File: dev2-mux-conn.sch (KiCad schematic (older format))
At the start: 9 parts, among them J26 Device 2, U16 TS12A44514, U17 TS12A44514, U20 MAX4533, U50 74LS32, U54 LTC1391, U55 LTC1391, U56 LTC1391

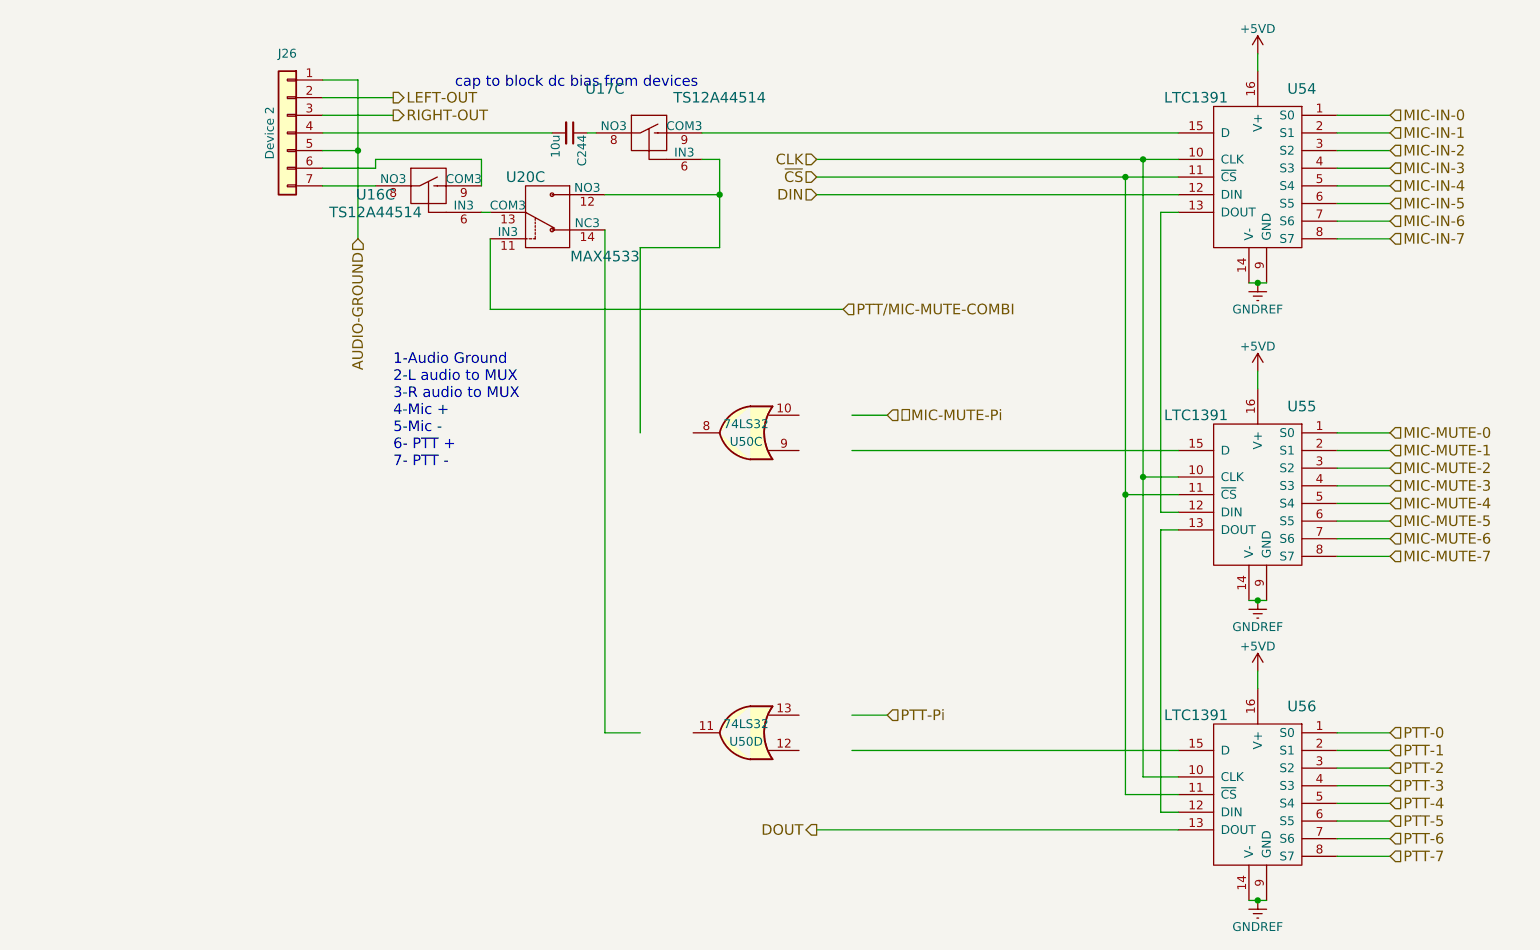
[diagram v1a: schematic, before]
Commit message: Updating power + libraries
- Reannotated all parts
- Migrated to new OR gate library
- Reorganized power sheet
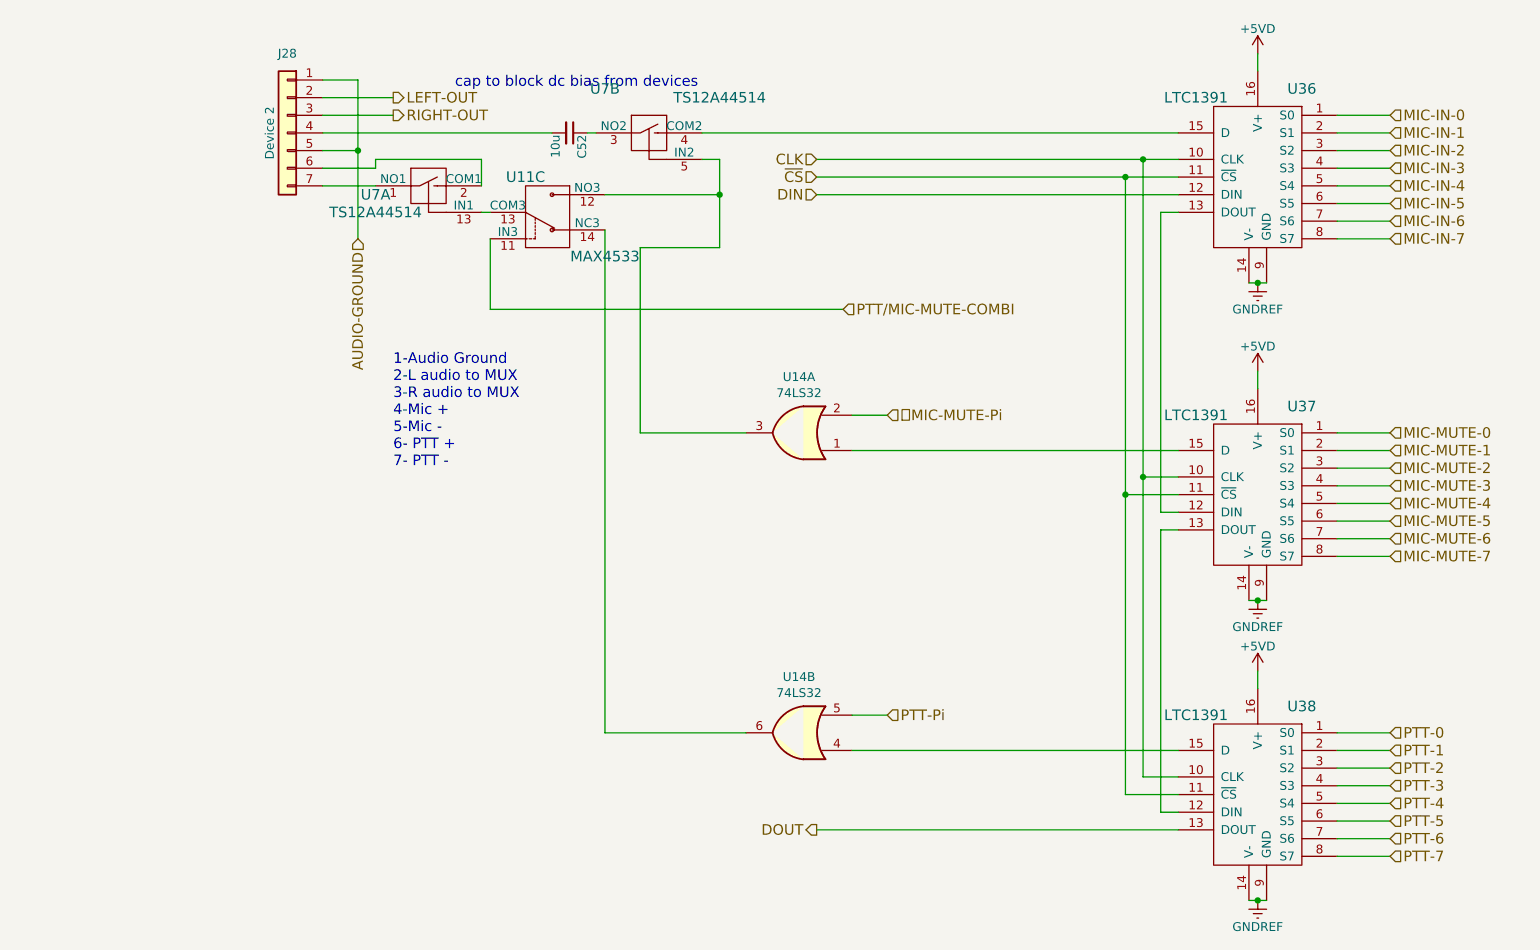
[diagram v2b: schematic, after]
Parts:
- removed U50: 74LS32, SMD_Packages:SSOP-14, symbol 74LS32
- added U14: 74LS32, symbol 74LS32
- renumbered C244 to C52, J26 to J28, U20 to U11, U54 to U36, U55 to U37, U56 to U38, U17 to U7, U16 to U7
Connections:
- wire segments 76 -> 77
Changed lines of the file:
@@
-EESchema Schematic File Version 2
+EESchema Schematic File Version 3
 LIBS:SW-Texas
 LIBS:power
@@
 $Descr USLetter 11000 8500
 encoding utf-8
-Sheet 16 15
+Sheet 7 15
 Title ""
 Date ""
@@
 $EndDescr
 $Comp
-L Conn_01x07 J26
+L Conn_01x07 J28
 U 1 1 58EAA0D9
 P 900 1150
-F 0 "J26" H 900 1600 50  0000 C CNN
+F 0 "J28" H 900 1600 50  0000 C CNN
 F 1 "Device 2" V 1000 1150 50  0000 C CNN
 F 2 "Pin_Headers:Pin_Header_Straight_1x07_Pitch2.54mm" H 900 1150 50  0001 C CNN
@@
 $Comp
 L TS12A44514 U?
-U 3 1 58EAA0E5
+U 2 1 58EAA0E5
 P 2950 1150
 AR Path="/58DEDA38/58EAA0E5" Ref="U?"  Part="1"
 AR Path="/58DEDA38/58E9E25B/58EAA0E5" Ref="U?"  Part="1"
-AR Path="/58DEDA38/58E9E991/58EAA0E5" Ref="U17"  Part="3"
-F 0 "U17" H 2700 1400 60  0000 C CNN
+AR Path="/58DEDA38/58E9E991/58EAA0E5" Ref="U7"  Part="2"
+F 0 "U7" H 2700 1400 60  0000 C CNN
 F 1 "TS12A44514" H 3350 1350 60  0000 C CNN
 F 2 "Housings_SSOP:TSSOP-14_4.4x5mm_Pitch0.65mm" H 3450 2450 60  0001 C CNN
@@
 F 7 "TSSOP14" H 3250 2350 60  0001 C CNN "Package ID"
 F 8 "0.00@0" H 3000 2150 60  0001 C CNN "Pricing"
-	3    2950 1150
+	2    2950 1150
 	1    0    0    -1
 $EndComp
 $Comp
 L TS12A44514 U?
-U 3 1 58EAA0F1
+U 1 1 58EAA0F1
 P 1700 1450
 AR Path="/58DEDA38/58EAA0F1" Ref="U?"  Part="1"
 AR Path="/58DEDA38/58E9E25B/58EAA0F1" Ref="U?"  Part="1"
-AR Path="/58DEDA38/58E9E991/58EAA0F1" Ref="U16"  Part="3"
-F 0 "U16" H 1400 1400 60  0000 C CNN
+AR Path="/58DEDA38/58E9E991/58EAA0F1" Ref="U7"  Part="1"
+F 0 "U7" H 1400 1400 60  0000 C CNN
 F 1 "TS12A44514" H 1400 1300 60  0000 C CNN
 F 2 "Housings_SSOP:TSSOP-14_4.4x5mm_Pitch0.65mm" H 2200 2750 60  0001 C CNN
@@
 F 7 "TSSOP14" H 2000 2650 60  0001 C CNN "Package ID"
 F 8 "0.00@0" H 1750 2450 60  0001 C CNN "Pricing"
-	3    1700 1450
-	1    0    0    -1
-$EndComp
-$Comp
-L C_Small C244
+	1    1700 1450
+	1    0    0    -1
+$EndComp
+$Comp
+L C_Small C52
 U 1 1 58EAA0F8
 P 2500 1150
-F 0 "C244" H 2510 1220 50  0000 L CNN
+F 0 "C52" H 2510 1220 50  0000 L CNN
 F 1 "10u" H 2510 1070 50  0000 L CNN
 F 2 "Capacitors_SMD:C_0603" H 2500 1150 50  0001 C CNN
@@
 AUDIO-GROUND
 $Comp
-L LTC1391 U54
+L LTC1391 U36
 U 1 1 58EAA108
 P 6400 1400
-F 0 "U54" H 6150 1900 60  0000 C CNN
+F 0 "U36" H 6150 1900 60  0000 C CNN
 F 1 "LTC1391" H 6750 1850 60  0000 C CNN
 F 2 "Housings_SSOP:SSOP-16_3.9x4.9mm_Pitch0.635mm" H 6500 2650 60  0001 C CNN
@@
 DOUT
 $Comp
-L +5VD #PWR0205
+L +5VD #PWR072
 U 1 1 58EAA113
 P 6400 700
-F 0 "#PWR0205" H 6400 550 50  0001 C CNN
+F 0 "#PWR072" H 6400 550 50  0001 C CNN
 F 1 "+5VD" H 6400 840 50  0000 C CNN
 F 2 "" H 6400 700 50  0001 C CNN
@@
 $EndComp
 $Comp
-L GNDREF #PWR0206
+L GNDREF #PWR073
 U 1 1 58EAA119
 P 6400 2000
-F 0 "#PWR0206" H 6400 1750 50  0001 C CNN
+F 0 "#PWR073" H 6400 1750 50  0001 C CNN
 F 1 "GNDREF" H 6400 1850 50  0000 C CNN
 F 2 "" H 6400 2000 50  0001 C CNN
@@
 Text HLabel 7150 1750 2    60   Input ~ 0
 MIC-IN-7
-$Comp
-L 74LS32 U50
-U 3 1 58EAA127
-P 3500 2850
-F 0 "U50" H 3500 2900 50  0000 C CNN
-F 1 "74LS32" H 3500 2800 50  0000 C CNN
-F 2 "SMD_Packages:SSOP-14" H 3500 2850 50  0001 C CNN
-F 3 "" H 3500 2850 50  0001 C CNN
-	3    3500 2850
-	-1   0    0    1
-$EndComp
-$Comp
-L 74LS32 U50
-U 4 1 58EAA12E
-P 3500 4550
-F 0 "U50" H 3500 4600 50  0000 C CNN
-F 1 "74LS32" H 3500 4500 50  0000 C CNN
-F 2 "SMD_Packages:SSOP-14" H 3500 4550 50  0001 C CNN
-F 3 "" H 3500 4550 50  0001 C CNN
-F 4 "0.00@0" H 3500 4550 60  0001 C CNN "Pricing"
-	4    3500 4550
-	-1   0    0    1
-$EndComp
 Text HLabel 4300 2750 2    60   Input ~ 0
 MIC-MUTE-Pi
@@
 P 2350 1600
 AR Path="/58DEDA38/58E9E25B/58EAA13B" Ref="U?"  Part="1"
-AR Path="/58DEDA38/58E9E991/58EAA13B" Ref="U20"  Part="3"
-F 0 "U20" H 2450 1800 60  0000 C CNN
+AR Path="/58DEDA38/58E9E991/58EAA13B" Ref="U11"  Part="3"
+F 0 "U11" H 2450 1800 60  0000 C CNN
 F 1 "MAX4533" H 2000 1350 60  0000 C CNN
 F 2 "Housings_SSOP:SSOP-20_4.4x6.5mm_Pitch0.65mm" H 2450 2550 60  0001 C CNN
@@
 PTT-7
 $Comp
-L LTC1391 U55
+L LTC1391 U37
 U 1 1 58EAA156
 P 6400 3200
-F 0 "U55" H 6150 3700 60  0000 C CNN
+F 0 "U37" H 6150 3700 60  0000 C CNN
 F 1 "LTC1391" H 6750 3650 60  0000 C CNN
 F 2 "Housings_SSOP:SSOP-16_3.9x4.9mm_Pitch0.635mm" H 6500 4450 60  0001 C CNN
@@
 $EndComp
 $Comp
-L +5VD #PWR0207
+L +5VD #PWR074
 U 1 1 58EAA15D
 P 6400 2500
-F 0 "#PWR0207" H 6400 2350 50  0001 C CNN
+F 0 "#PWR074" H 6400 2350 50  0001 C CNN
 F 1 "+5VD" H 6400 2640 50  0000 C CNN
 F 2 "" H 6400 2500 50  0001 C CNN
@@
 $EndComp
 $Comp
-L GNDREF #PWR0208
+L GNDREF #PWR075
 U 1 1 58EAA163
 P 6400 3800
-F 0 "#PWR0208" H 6400 3550 50  0001 C CNN
+F 0 "#PWR075" H 6400 3550 50  0001 C CNN
 F 1 "GNDREF" H 6400 3650 50  0000 C CNN
 F 2 "" H 6400 3800 50  0001 C CNN
@@
 $EndComp
 $Comp
-L LTC1391 U56
+L LTC1391 U38
 U 1 1 58EAA16D
 P 6400 4900
-F 0 "U56" H 6150 5400 60  0000 C CNN
+F 0 "U38" H 6150 5400 60  0000 C CNN
 F 1 "LTC1391" H 6750 5350 60  0000 C CNN
 F 2 "Housings_SSOP:SSOP-16_3.9x4.9mm_Pitch0.635mm" H 6500 6150 60  0001 C CNN
@@
 $EndComp
 $Comp
-L +5VD #PWR0209
+L +5VD #PWR076
 U 1 1 58EAA174
 P 6400 4200
-F 0 "#PWR0209" H 6400 4050 50  0001 C CNN
+F 0 "#PWR076" H 6400 4050 50  0001 C CNN
 F 1 "+5VD" H 6400 4340 50  0000 C CNN
 F 2 "" H 6400 4200 50  0001 C CNN
@@
 $EndComp
 $Comp
-L GNDREF #PWR0210
+L GNDREF #PWR077
 U 1 1 58EAA17A
 P 6400 5500
-F 0 "#PWR0210" H 6400 5250 50  0001 C CNN
+F 0 "#PWR077" H 6400 5250 50  0001 C CNN
 F 1 "GNDREF" H 6400 5350 50  0000 C CNN
 F 2 "" H 6400 5500 50  0001 C CNN
@@
 	2900 1800 2900 2850
 Wire Wire Line
-	4100 2750 4300 2750
-Wire Wire Line
 	4100 4450 4300 4450
 Wire Wire Line
 	2700 1500 3350 1500
 Connection ~ 3350 1500
-Wire Wire Line
-	2900 4550 2700 4550
 Wire Wire Line
 	2700 4550 2700 1700
@@
 Text Notes 1500 3050 0    60   ~ 0
 1-Audio Ground\n2-L audio to MUX\n3-R audio to MUX\n4-Mic +\n5-Mic -\n6- PTT +\n7- PTT -
+Wire Wire Line
+	2700 4550 3500 4550
+$Comp
+L 74LS32 U?
+U 1 1 59D24FEE
+P 3800 2850
+AR Path="/58DEDA38/58E9E2BE/59D24FEE" Ref="U?"  Part="1"
+AR Path="/58DEDA38/58E9E991/59D24FEE" Ref="U14"  Part="1"
+F 0 "U14" H 3800 2533 50  0000 C CNN
+F 1 "74LS32" H 3800 2624 50  0000 C CNN
+F 2 "" H 3800 2850 50  0001 C CNN
+F 3 "" H 3800 2850 50  0001 C CNN
+	1    3800 2850
+	-1   0    0    1
+$EndComp
+Wire Wire Line
+	2900 2850 3500 2850
+$Comp
+L 74LS32 U?
+U 2 1 59D24FF6
+P 3800 4550
+AR Path="/58DEDA38/58E9E2BE/59D24FF6" Ref="U?"  Part="2"
+AR Path="/58DEDA38/58E9E9F4/59D24FF6" Ref="U?"  Part="2"
+AR Path="/58DEDA38/58E9E991/59D24FF6" Ref="U14"  Part="2"
+F 0 "U14" H 3800 4233 50  0000 C CNN
+F 1 "74LS32" H 3800 4324 50  0000 C CNN
+F 2 "" H 3800 4550 50  0001 C CNN
+F 3 "" H 3800 4550 50  0001 C CNN
+	2    3800 4550
+	-1   0    0    1
+$EndComp
+Wire Wire Line
+	4300 2750 4100 2750
 $EndSCHEMATC

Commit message: Updates during pcb layout
Added more net labels
moved switches and OR gates to +5V instead of +5VD
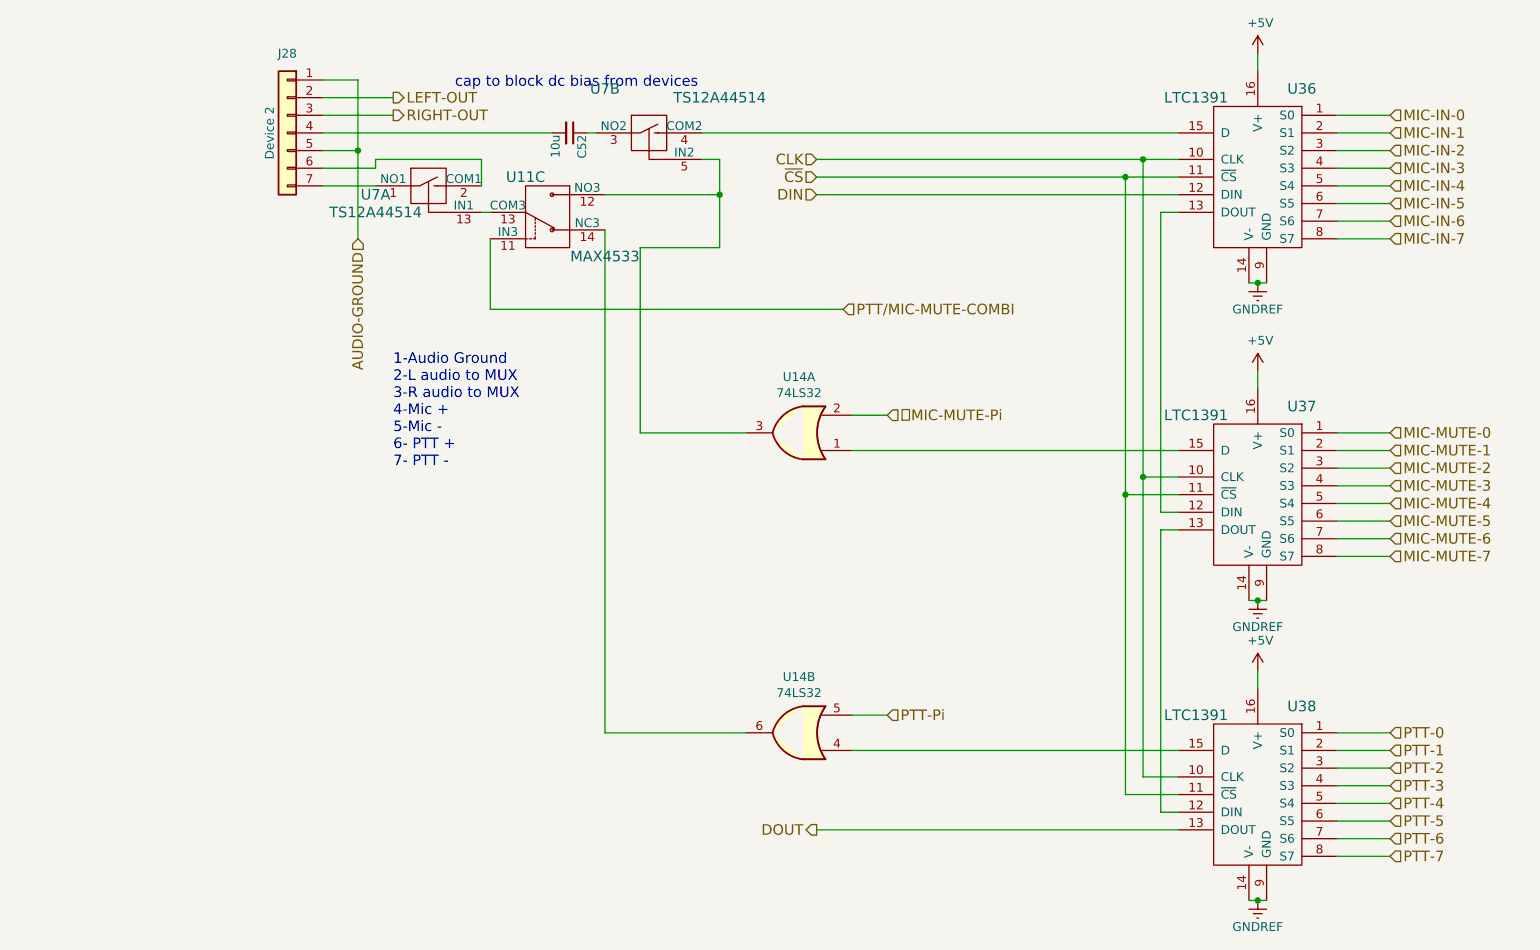
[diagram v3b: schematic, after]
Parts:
- J28: footprint Pin_Headers:Pin_Header_Straight_1x07_Pitch2.54mm -> SW-TEConn:3-794681-8
- U14: footprint (none) -> Housings_SSOP:SSOP-14_5.3x6.2mm_Pitch0.65mm
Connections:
- net +5VD renamed +5V
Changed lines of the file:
@@
 LIBS:SW-Diodes-Inc
 LIBS:interface
+LIBS:SW-gElectroMech
 LIBS:edc-mux-board-cache
 EELAYER 26 0
@@
 F 0 "J28" H 900 1600 50  0000 C CNN
 F 1 "Device 2" V 1000 1150 50  0000 C CNN
-F 2 "Pin_Headers:Pin_Header_Straight_1x07_Pitch2.54mm" H 900 1150 50  0001 C CNN
+F 2 "SW-TEConn:3-794681-8" H 900 1150 50  0001 C CNN
 F 3 "" H 900 1150 50  0001 C CNN
 F 4 "0.00@0" H 900 1150 60  0001 C CNN "Pricing"
@@
 Text HLabel 3900 5100 0    60   Output ~ 0
 DOUT
-$Comp
-L +5VD #PWR072
-U 1 1 58EAA113
-P 6400 700
-F 0 "#PWR072" H 6400 550 50  0001 C CNN
-F 1 "+5VD" H 6400 840 50  0000 C CNN
-F 2 "" H 6400 700 50  0001 C CNN
-F 3 "" H 6400 700 50  0001 C CNN
-	1    6400 700
-	1    0    0    -1
-$EndComp
 $Comp
 L GNDREF #PWR073
@@
 $EndComp
 $Comp
-L +5VD #PWR074
-U 1 1 58EAA15D
-P 6400 2500
-F 0 "#PWR074" H 6400 2350 50  0001 C CNN
-F 1 "+5VD" H 6400 2640 50  0000 C CNN
-F 2 "" H 6400 2500 50  0001 C CNN
-F 3 "" H 6400 2500 50  0001 C CNN
-	1    6400 2500
-	1    0    0    -1
-$EndComp
-$Comp
 L GNDREF #PWR075
 U 1 1 58EAA163
@@
 $EndComp
 $Comp
-L +5VD #PWR076
-U 1 1 58EAA174
-P 6400 4200
-F 0 "#PWR076" H 6400 4050 50  0001 C CNN
-F 1 "+5VD" H 6400 4340 50  0000 C CNN
-F 2 "" H 6400 4200 50  0001 C CNN
-F 3 "" H 6400 4200 50  0001 C CNN
-	1    6400 4200
-	1    0    0    -1
-$EndComp
-$Comp
 L GNDREF #PWR077
 U 1 1 58EAA17A
@@
 $EndComp
 Wire Wire Line
-	1300 850  1300 1750
+	1300 850  1300 1250
+Wire Wire Line
+	1300 1250 1300 1750
 Wire Wire Line
 	1100 850  1300 850
@@
 	3900 1500 5950 1500
 Wire Wire Line
-	3900 1400 5950 1400
-Wire Wire Line
-	3900 1300 5950 1300
+	3900 1400 5650 1400
+Wire Wire Line
+	5650 1400 5950 1400
+Wire Wire Line
+	3900 1300 5750 1300
+Wire Wire Line
+	5750 1300 5950 1300
 Wire Wire Line
 	6400 700  6400 800
 Wire Wire Line
-	6350 2000 6450 2000
+	6350 2000 6400 2000
+Wire Wire Line
+	6400 2000 6450 2000
 Wire Wire Line
 	6400 2000 6400 2000
 Connection ~ 6400 2000
 Wire Wire Line
-	3350 1300 3350 1800
+	3350 1300 3350 1500
+Wire Wire Line
+	3350 1500 3350 1800
 Wire Wire Line
 	3350 1800 2900 1800
@@
 	6400 2500 6400 2600
 Wire Wire Line
-	6350 3800 6450 3800
+	6350 3800 6400 3800
+Wire Wire Line
+	6400 3800 6450 3800
 Wire Wire Line
 	6400 3800 6400 3800
@@
 	6400 4200 6400 4300
 Wire Wire Line
-	6350 5500 6450 5500
+	6350 5500 6400 5500
+Wire Wire Line
+	6400 5500 6450 5500
 Wire Wire Line
 	6400 5500 6400 5500
 Connection ~ 6400 5500
 Wire Wire Line
-	5750 1300 5750 4800
+	5750 1300 5750 3100
+Wire Wire Line
+	5750 3100 5750 4800
 Connection ~ 5750 3100
 Connection ~ 5750 1300
 Wire Wire Line
-	5650 1400 5650 4900
+	5650 1400 5650 3200
+Wire Wire Line
+	5650 3200 5650 4900
 Connection ~ 5650 3200
 Connection ~ 5650 1400
@@
 F 0 "U14" H 3800 2533 50  0000 C CNN
 F 1 "74LS32" H 3800 2624 50  0000 C CNN
-F 2 "" H 3800 2850 50  0001 C CNN
+F 2 "Housings_SSOP:SSOP-14_5.3x6.2mm_Pitch0.65mm" H 3800 2850 50  0001 C CNN
 F 3 "" H 3800 2850 50  0001 C CNN
 	1    3800 2850
@@
 F 0 "U14" H 3800 4233 50  0000 C CNN
 F 1 "74LS32" H 3800 4324 50  0000 C CNN
-F 2 "" H 3800 4550 50  0001 C CNN
+F 2 "Housings_SSOP:SSOP-14_5.3x6.2mm_Pitch0.65mm" H 3800 4550 50  0001 C CNN
 F 3 "" H 3800 4550 50  0001 C CNN
 	2    3800 4550
@@
 Wire Wire Line
 	4300 2750 4100 2750
+$Comp
+L +5V #PWR?
+U 1 1 59D25E17
+P 6400 700
+F 0 "#PWR?" H 6400 550 50  0001 C CNN
+F 1 "+5V" H 6415 873 50  0000 C CNN
+F 2 "" H 6400 700 50  0001 C CNN
+F 3 "" H 6400 700 50  0001 C CNN
+	1    6400 700
+	1    0    0    -1
+$EndComp
+$Comp
+L +5V #PWR?
+U 1 1 59D25EDD
+P 6400 2500
+F 0 "#PWR?" H 6400 2350 50  0001 C CNN
+F 1 "+5V" H 6415 2673 50  0000 C CNN
+F 2 "" H 6400 2500 50  0001 C CNN
+F 3 "" H 6400 2500 50  0001 C CNN
+	1    6400 2500
+	1    0    0    -1
+$EndComp
+$Comp
+L +5V #PWR?
+U 1 1 59D25FCF
+P 6400 4200
+F 0 "#PWR?" H 6400 4050 50  0001 C CNN
+F 1 "+5V" H 6415 4373 50  0000 C CNN
+F 2 "" H 6400 4200 50  0001 C CNN
+F 3 "" H 6400 4200 50  0001 C CNN
+	1    6400 4200
+	1    0    0    -1
+$EndComp
 $EndSCHEMATC

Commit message: Lots of progress on PCB
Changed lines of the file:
@@
 $EndComp
 Wire Wire Line
-	1300 850  1300 1250
-Wire Wire Line
-	1300 1250 1300 1750
+	1300 850  1300 1750
 Wire Wire Line
 	1100 850  1300 850
@@
 	3900 1500 5950 1500
 Wire Wire Line
-	3900 1400 5650 1400
-Wire Wire Line
-	5650 1400 5950 1400
-Wire Wire Line
-	3900 1300 5750 1300
-Wire Wire Line
-	5750 1300 5950 1300
+	3900 1400 5950 1400
+Wire Wire Line
+	3900 1300 5950 1300
 Wire Wire Line
 	6400 700  6400 800
 Wire Wire Line
-	6350 2000 6400 2000
-Wire Wire Line
-	6400 2000 6450 2000
+	6350 2000 6450 2000
 Wire Wire Line
 	6400 2000 6400 2000
 Connection ~ 6400 2000
 Wire Wire Line
-	3350 1300 3350 1500
-Wire Wire Line
-	3350 1500 3350 1800
+	3350 1300 3350 1800
 Wire Wire Line
 	3350 1800 2900 1800
@@
 	6400 2500 6400 2600
 Wire Wire Line
-	6350 3800 6400 3800
-Wire Wire Line
-	6400 3800 6450 3800
+	6350 3800 6450 3800
 Wire Wire Line
 	6400 3800 6400 3800
@@
 	6400 4200 6400 4300
 Wire Wire Line
-	6350 5500 6400 5500
-Wire Wire Line
-	6400 5500 6450 5500
+	6350 5500 6450 5500
 Wire Wire Line
 	6400 5500 6400 5500
 Connection ~ 6400 5500
 Wire Wire Line
-	5750 1300 5750 3100
-Wire Wire Line
-	5750 3100 5750 4800
+	5750 1300 5750 4800
 Connection ~ 5750 3100
 Connection ~ 5750 1300
 Wire Wire Line
-	5650 1400 5650 3200
-Wire Wire Line
-	5650 3200 5650 4900
+	5650 1400 5650 4900
 Connection ~ 5650 3200
 Connection ~ 5650 1400
@@
 	4300 2750 4100 2750
 $Comp
-L +5V #PWR?
+L +5V #PWR072
 U 1 1 59D25E17
 P 6400 700
-F 0 "#PWR?" H 6400 550 50  0001 C CNN
+F 0 "#PWR072" H 6400 550 50  0001 C CNN
 F 1 "+5V" H 6415 873 50  0000 C CNN
 F 2 "" H 6400 700 50  0001 C CNN
@@
 $EndComp
 $Comp
-L +5V #PWR?
+L +5V #PWR074
 U 1 1 59D25EDD
 P 6400 2500
-F 0 "#PWR?" H 6400 2350 50  0001 C CNN
+F 0 "#PWR074" H 6400 2350 50  0001 C CNN
 F 1 "+5V" H 6415 2673 50  0000 C CNN
 F 2 "" H 6400 2500 50  0001 C CNN
@@
 $EndComp
 $Comp
-L +5V #PWR?
+L +5V #PWR076
 U 1 1 59D25FCF
 P 6400 4200
-F 0 "#PWR?" H 6400 4050 50  0001 C CNN
+F 0 "#PWR076" H 6400 4050 50  0001 C CNN
 F 1 "+5V" H 6415 4373 50  0000 C CNN
 F 2 "" H 6400 4200 50  0001 C CNN
